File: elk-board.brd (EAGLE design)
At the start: 55 x 25.6 mm, 201 parts, among them IC1 KLM8G1GESD-B03P, IC10 MP2143DJ-LF-P, IC2 ALLWINNER--H3, IC3 SY6280, IC4 K4B4G1646D-BCK0, IC5 RT8059GJ5, IC6 RT8059GJ5, IC7 SY8089A, IC8 NCP803SN263T1G, IC9 RT8059GJ5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

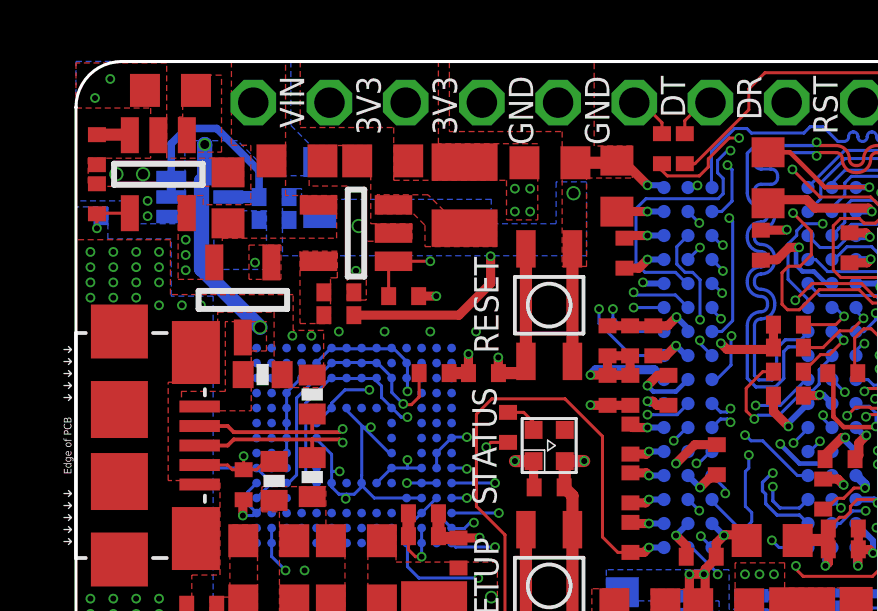
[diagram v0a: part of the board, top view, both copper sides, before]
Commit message: Decrease LEDs brightness + MCU_REG_ON (Pull Down)
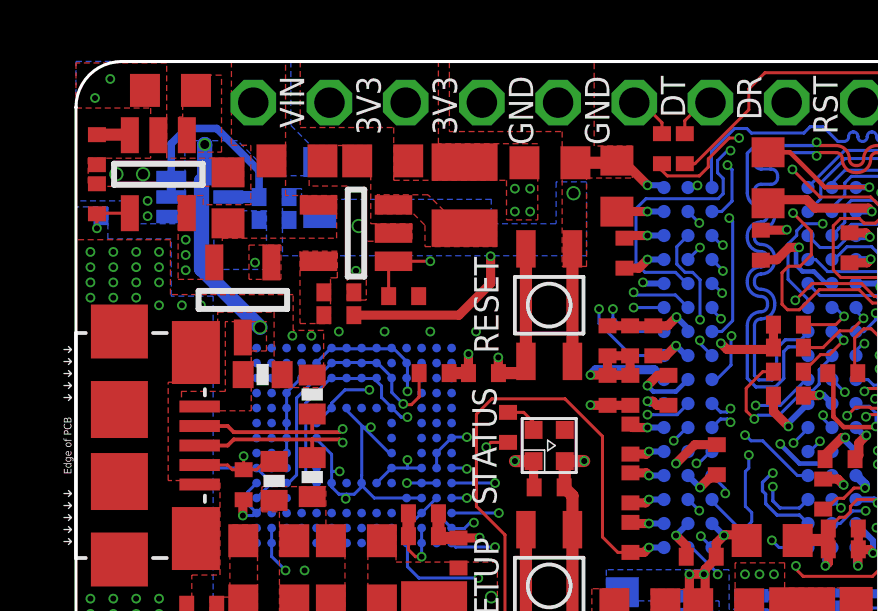
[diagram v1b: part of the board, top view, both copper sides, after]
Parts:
- R37, R41, R42: value 1K ohm -> 1.5K ohm
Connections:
- net 3.3V: no longer R21.2
- net GND: now also R21.2
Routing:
- net 3.3V: track 75.2 -> 74.6 mm, vias 33 -> 32

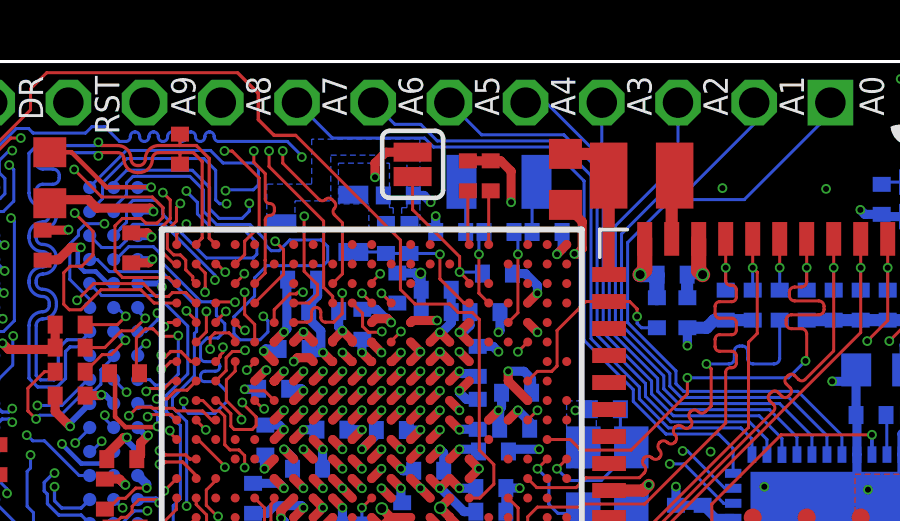
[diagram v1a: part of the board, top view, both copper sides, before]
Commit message: CONNECT UBOOT WITH SETUP Button
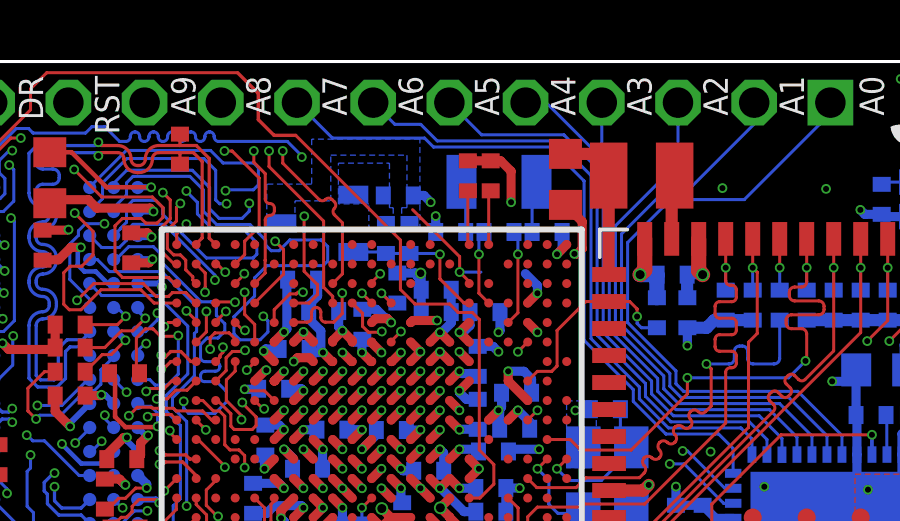
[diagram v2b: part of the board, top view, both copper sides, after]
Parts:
- removed JP1: JUMPER-SMT_2_NO_SILK, SparkFun-Jumpers:SMT-JUMPER_2_NO_SILK
- removed R36: 10K ohm, GHI-BasicComponents:0402
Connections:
- removed net UBOOT: IC2.W6, JP1.2, R36.2
- net 3.3V: no longer R36.1
- net GND: no longer JP1.1
- net SETUP_SW: now also IC2.W6
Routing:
- net UBOOT: track 5.13 -> 0.00 mm, vias 1 -> 0
- net SETUP_SW: track 29.3 -> 33.2 mm, vias 2 -> 3
- net GND: track 199.0 -> 197.1 mm, vias 224 -> 223
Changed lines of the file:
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@@
 <attribute name="NAME" x="43.3197" y="15.4226" size="0.6096" layer="139" font="vector" ratio="15" rot="MR270" align="center"/>
 </element>
-<element name="R36" library="GHI-BasicComponents" package="0402" value="10K ohm" x="37.9916" y="18.5314" smashed="yes" rot="MR0">
-<attribute name="NAME" x="39.6299" y="18.5314" size="0.6096" layer="139" font="vector" ratio="15" rot="MR0" align="center"/>
-</element>
 <element name="R2" library="GHI-BasicComponents" package="0402" value="30K ohm" x="50.1" y="17.48" smashed="yes" rot="MR90">
 <attribute name="NAME" x="50.2143" y="16.3116" size="0.6096" layer="139" font="vector" ratio="15" rot="MR90" align="center"/>
@@
 <attribute name="NAME" x="11.93165" y="14.8576" size="0.6096" layer="138" font="vector" ratio="15" align="bottom-center"/>
 </element>
-<element name="JP1" library="SparkFun-Jumpers" library_urn="urn:adsk.eagle:library:528" package="SMT-JUMPER_2_NO_SILK" package3d_urn="urn:adsk.eagle:package:39279/1" value="JUMPER-SMT_2_NO_SILK" x="35.1634" y="22.171" smashed="yes" rot="R270"/>
 <element name="C92" library="GHI-BasicComponents" package="0402" value="100nF" x="19.7485" y="14.6396" smashed="yes" rot="R270">
 <attribute name="NAME" x="20.2805" y="14.6396" size="0.6096" layer="138" font="vector" ratio="15" rot="R270" align="bottom-center"/>
@@
 <contactref element="JP3" pad="15"/>
 <contactref element="JP3" pad="14"/>
-<contactref element="JP1" pad="1"/>
 <via x="33.475" y="15.8996" extent="1-16" drill="0.2"/>
 <via x="34.125" y="15.8996" extent="1-16" drill="0.2"/>
@@
 <wire x1="31.6993" y1="17.2826" x2="31.6993" y2="17.4858" width="0.3048" layer="16"/>
 <wire x1="31.998" y1="17.7845" x2="31.998" y2="18.329" width="0.3048" layer="16"/>
-<wire x1="35.1634" y1="22.5774" x2="34.2741" y2="22.5774" width="0.3048" layer="1"/>
-<wire x1="34.2741" y1="22.5774" x2="33.909" y2="22.2123" width="0.3048" layer="1"/>
-<wire x1="33.909" y1="21.7424" x2="33.909" y2="22.2123" width="0.3048" layer="1"/>
-<via x="33.909" y="21.7424" extent="1-16" drill="0.2"/>
 <wire x1="32.10515" y1="16.62275" x2="31.6993" y2="17.0286" width="0.3048" layer="16"/>
 <wire x1="31.6993" y1="17.2826" x2="31.6993" y2="17.0286" width="0.3048" layer="16"/>
@@
 <wire x1="34.2744" y1="20.202" x2="35.9334" y2="20.447" width="0" layer="19" extent="16-16"/>
 <wire x1="34.1866" y1="21.136" x2="34.2744" y2="20.202" width="0" layer="19" extent="16-16"/>
-<wire x1="33.909" y1="21.7424" x2="34.1866" y2="21.136" width="0" layer="19" extent="1-16"/>
-<wire x1="33.1884" y1="21.162" x2="33.909" y2="21.7424" width="0" layer="19" extent="1-16"/>
+<wire x1="33.1884" y1="21.162" x2="34.1866" y2="21.136" width="0" layer="19" extent="16-16"/>
 <wire x1="35.5092" y1="6.0452" x2="35.013" y2="7.874" width="0" layer="19" extent="16-16"/>
 <wire x1="35.5092" y1="4.7452" x2="35.5092" y2="6.0452" width="0" layer="19" extent="1-1"/>
@@
 <contactref element="LED2" pad="A"/>
 <contactref element="R31" pad="1"/>
-<contactref element="R36" pad="1"/>
 <contactref element="C5" pad="1"/>
 <contactref element="C8" pad="1"/>
@@
 <wire x1="39.325" y1="17.875" x2="39.325" y2="18.129" width="0.3048" layer="16"/>
 <wire x1="39.325" y1="18.129" x2="38.9226" y2="18.5314" width="0.3048" layer="16"/>
-<wire x1="38.9226" y1="18.5314" x2="38.4916" y2="18.5314" width="0.3048" layer="16"/>
 <wire x1="43.307" y1="17.726" x2="43.307" y2="18.488" width="0.508" layer="16"/>
 <wire x1="43.307" y1="18.488" x2="43.315" y2="18.496" width="0.4064" layer="16"/>
@@
 <wire x1="30.5881" y1="8.4582" x2="31.369" y2="7.577" width="0" layer="19" extent="16-16"/>
 <wire x1="33.313" y1="7.874" x2="31.7738" y2="8.4582" width="0" layer="19" extent="16-16"/>
-<wire x1="38.4459" y1="20.9108" x2="38.4916" y2="18.5314" width="0" layer="19" extent="16-16"/>
+<wire x1="38.4459" y1="20.9108" x2="38.9226" y2="18.5314" width="0" layer="19" extent="16-16"/>
 <wire x1="35.766821875" y1="20.911021875" x2="37.0049" y2="22.29" width="0" layer="19" extent="1-1"/>
 <wire x1="35.0604" y1="20.202" x2="35.1866" y2="21.136" width="0" layer="19" extent="16-16"/>
@@
 <wire x1="38.675" y1="19.7869" x2="38.675" y2="19.175" width="0.1016" layer="16"/>
 </signal>
-<signal name="UBOOT">
-<contactref element="R36" pad="2"/>
-<contactref element="JP1" pad="2"/>
-<via x="36.73135" y="18.58215" extent="1-16" drill="0.2"/>
-<wire x1="37.05" y1="18.2" x2="37.05" y2="18.2635" width="0.1016" layer="1"/>
-<wire x1="37.05" y1="18.2635" x2="36.73135" y2="18.58215" width="0.1016" layer="1"/>
-<contactref element="IC2" pad="W6"/>
-<wire x1="37.4916" y1="18.5314" x2="37.44085" y2="18.58215" width="0.1016" layer="16"/>
-<wire x1="37.44085" y1="18.58215" x2="36.73135" y2="18.58215" width="0.1016" layer="16"/>
-<wire x1="36.73135" y1="18.58215" x2="36.73135" y2="19.09345" width="0.1016" layer="1"/>
-<wire x1="36.73135" y1="19.09345" x2="35.1634" y2="20.6614" width="0.1016" layer="1"/>
-<wire x1="35.1634" y1="20.6614" x2="35.1634" y2="21.7646" width="0.1016" layer="1"/>
-</signal>
 <signal name="AP_RESET#">
 <contactref element="IC8" pad="2"/>
@@
 <wire x1="31.234196875" y1="3.478346875" x2="31.615196875" y2="3.478346875" width="0.1016" layer="14"/>
 <wire x1="31.234196875" y1="3.478346875" x2="31.14624375" y2="3.5663" width="0.1016" layer="14"/>
+<via x="36.73135" y="18.58215" extent="1-16" drill="0.2"/>
+<wire x1="37.05" y1="18.2" x2="37.05" y2="18.2635" width="0.1016" layer="1"/>
+<wire x1="37.05" y1="18.2635" x2="36.73135" y2="18.58215" width="0.1016" layer="1"/>
+<contactref element="IC2" pad="W6"/>
+<wire x1="37.44085" y1="18.58215" x2="36.73135" y2="18.58215" width="0.1016" layer="16"/>
+<wire x1="36.73135" y1="18.58215" x2="36.73135" y2="19.09345" width="0.1016" layer="1"/>
+<wire x1="36.73135" y1="19.09345" x2="35.1634" y2="20.6614" width="0.1016" layer="1"/>
+<wire x1="32.5" y1="6.5" x2="37.05" y2="18.2" width="0" layer="19" extent="1-1"/>
 </signal>
 <signal name="N$21">

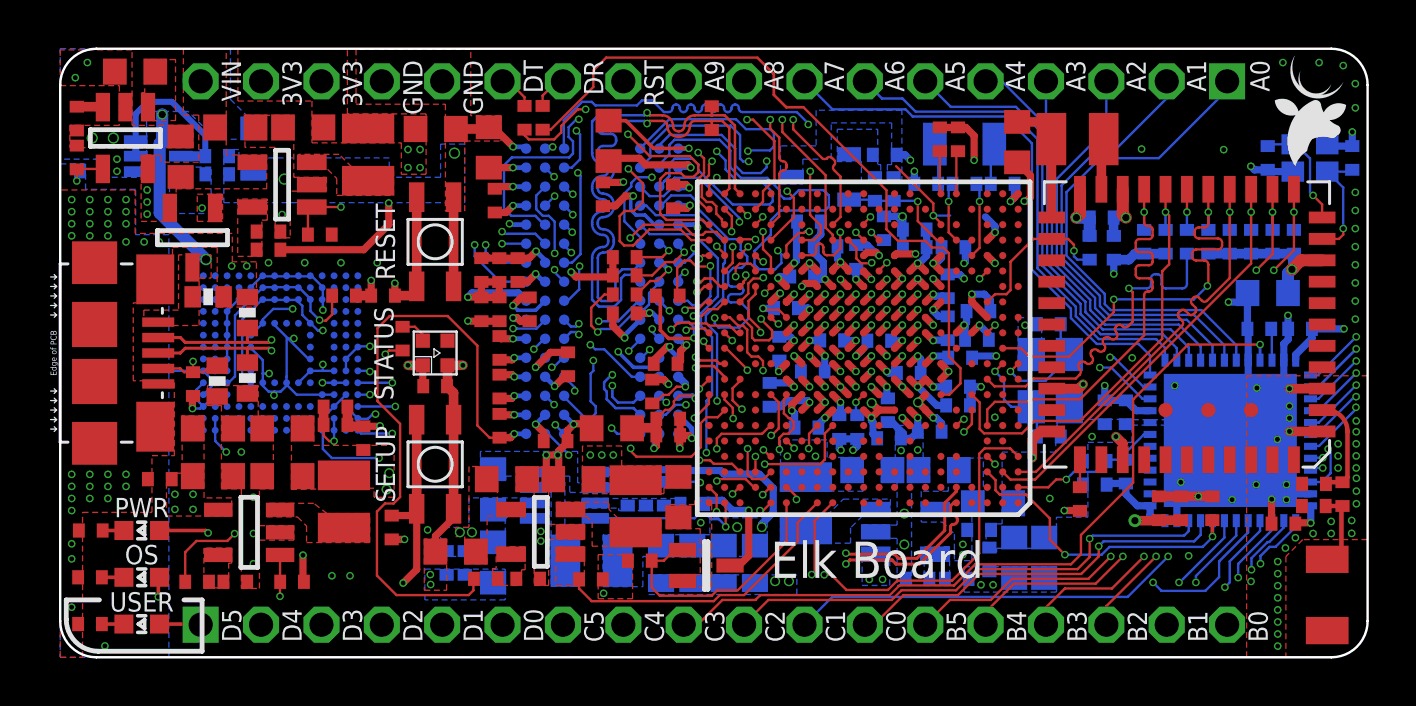
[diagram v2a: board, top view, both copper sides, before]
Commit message: Did UBOOT Push Button layout
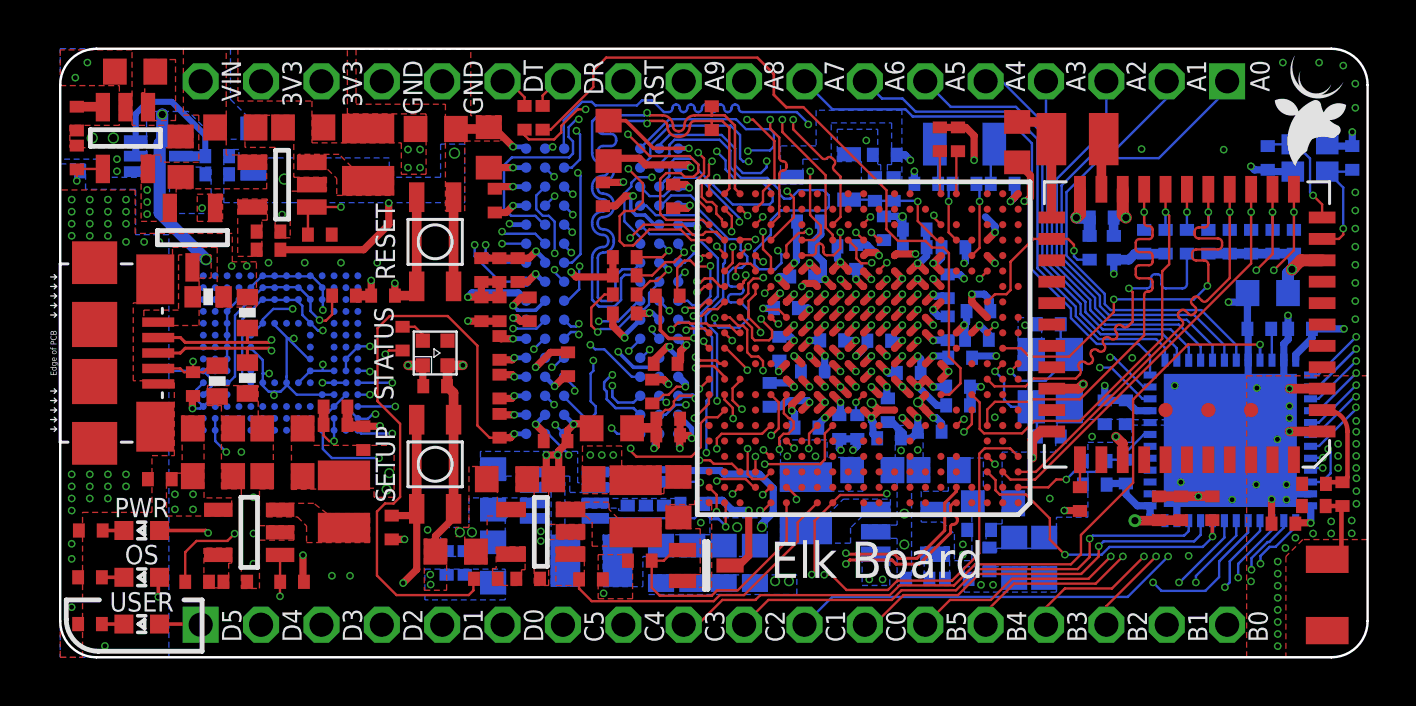
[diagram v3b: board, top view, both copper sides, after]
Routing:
- net SETUP_SW: track 33.2 -> 45.3 mm, vias 3 -> 4
- net GND: vias 223 -> 224
